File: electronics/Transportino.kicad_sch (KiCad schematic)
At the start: 44 parts

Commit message: Changed components and added new ones
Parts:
- removed C? (x10): 0.1u, symbol Device:C
- removed C? (x2): 1u, symbol Device:C
- removed J?: USB_B, symbol Connector:USB_B
- removed R? (x2): 27.4, symbol Device:R
- removed U?: RP2040, QFN40P700X700X90-57N, symbol RP2040:RP2040
- added BZ1: BUZZ, Buzzer_Beeper:Buzzer_12x9.5RM7.6, symbol Device:Buzzer
- added C1, C10, C11, C12, C14, C16, C23, C24, C5, C7, C8, C9: 0.1u, Capacitor_SMD:C_1206_3216Metric, symbol Device:C
- added C13, C15: 1u, Capacitor_SMD:C_1206_3216Metric, symbol Device:C
- added C20: 10n, Capacitor_SMD:C_1206_3216Metric, symbol Device:C
- added C26: 2.2n, Capacitor_SMD:C_1206_3216Metric, symbol Device:C
- added D2: STATUS, LED_SMD:LED_1206_3216Metric, symbol Device:LED
- added J1: MOTOR_A_0, Connector_JST:JST_XH_B3B-XH-A_1x03_P2.50mm_Vertical, symbol Connector:Conn_01x03_Female
- added J2: MOTOR_A_1, Connector_JST:JST_XH_B3B-XH-A_1x03_P2.50mm_Vertical, symbol Connector:Conn_01x03_Female
- added J3: MOTOR_B_0, Connector_JST:JST_XH_B3B-XH-A_1x03_P2.50mm_Vertical, symbol Connector:Conn_01x03_Female
- added J4: MOTOR_B_1, Connector_JST:JST_XH_B3B-XH-A_1x03_P2.50mm_Vertical, symbol Connector:Conn_01x03_Female
- added J5: USB_B_Micro, Connector_USB:USB_Micro-B_Amphenol_10118194_Horizontal, symbol Connector:USB_B_Micro
- added R1, R2: 27.4, Resistor_SMD:R_1206_3216Metric, symbol Device:R
- added R6: 1k, Resistor_SMD:R_1206_3216Metric, symbol Device:R
- added U1: RP2040, Package_DFN_QFN:QFN-56_EP_7.75x7.75_Pitch0.4mm, symbol RP2040:RP2040
- added U4: MPU-6050, Sensor_Motion:InvenSense_QFN-24_4x4mm_P0.5mm, symbol Sensor_Motion:MPU-6050
- BT1: renamed from BT?; footprint (none) -> Connector_JST:JST_XH_B2B-XH-A_1x02_P2.50mm_Vertical
- C17, C18, C19, C2, C22, C25, C4: renamed from C?; footprint (none) -> Capacitor_SMD:C_1206_3216Metric
- C21: renamed from C?; footprint (none) -> Capacitor_SMD:C_Elec_6.3x5.4
- C27: renamed from C?; footprint (none) -> Capacitor_SMD:C_Elec_8x10.2
- C3, C6: renamed from C?; footprint (none) -> Capacitor_SMD:CP_Elec_4x5.4
- D1: renamed from D?; value LED -> POWER; footprint (none) -> LED_SMD:LED_1206_3216Metric
- D3: renamed from D?; footprint DIOM6859X262N -> Diode_SMD:D_SMA
- L1: renamed from L?; footprint (none) -> Inductor_SMD:L_6.3x6.3_H3
- R3, R4, R7, R8, R9: renamed from R?; footprint (none) -> Resistor_SMD:R_1206_3216Metric
- R5: renamed from R?; value 4.7k -> 1k; footprint (none) -> Resistor_SMD:R_1206_3216Metric
- SW1: renamed from SW?; value SW_Push -> PROG; footprint (none) -> Button_Switch_SMD:SW_Push_SPST_NO_Alps_SKRK
- SW2: renamed from SW?; footprint (none) -> Button_Switch_THT:SW_CuK_OS102011MA1QN1_SPDT_Angled
- Y1: renamed from Y?; footprint (none) -> Crystal:Crystal_SMD_5032-4Pin_5.0x3.2mm
- gave numbers to parts that had none: 4
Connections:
- net +BATT is gone; now on net +12V: C21.1, U5.1 (VIN)
- net +1V1: now also C11.2, C13.2, C5.2, U1.23 (DVDD), U1.45 (VREG_VOUT), U1.50 (DVDD)
- net +3V3: now also D1.2 (A), C1.2, C10.2, C12.2, C14.2, C15.2, C16.2, C20.2, C23.2, C7.2, C8.2, C9.2, J2.2 (Pin_2), J4.2 (Pin_2), U1.1 (IOVDD), U1.10 (IOVDD), U1.22 (IOVDD), U1.33 (IOVDD), U1.42 (IOVDD), U1.43 (ADC_AVDD), U1.44 (VREG_VIN), U1.48 (USB_VDD), U1.49 (IOVDD), U4.13 (VDD), U4.8 (VDDIO)
- net +5V: no longer D1.1 (K)
- net CtrlA0: now also U1.28 (GPIO17)
- net CtrlA1: now also U1.29 (GPIO18)
- net CtrlAPWM: now also U1.27 (GPIO16)
- net CtrlB0: now also U1.34 (GPIO22)
- net CtrlB1: now also U1.35 (GPIO23)
- net CtrlBPWM: now also U1.32 (GPIO21)
- net DRV_EN: now also U1.18 (GPIO15)
- net GND: now also BZ1.2 (+), C1.1, C10.1, C11.1, C12.1, C13.1, C14.1, C15.1, C16.1, C20.1, C23.1, C24.1, C26.2, C5.1, C7.1, C8.1, C9.1, J2.3 (Pin_3), J4.3 (Pin_3), J5.5 (GND), J5.6 (Shield), R6.2, U1.19 (TESTEN), U1.57 (GND), U4.1 (CLKIN), U4.11 (FSYNC), U4.18 (GND)
- net MotorA0: now also J1.1 (Pin_1)
- net MotorA1: now also J1.2 (Pin_2)
- net MotorB0: now also J3.1 (Pin_1)
- net MotorB1: now also J3.2 (Pin_2)
- net QSPI_CSN: now also U1.56 (QSPI_SS_N)
- net QSPI_SCLK: now also U1.52 (QSPI_SCLK)
- net QSPI_SD0: now also U1.53 (QSPI_SD0)
- net QSPI_SD1: now also U1.55 (QSPI_SD1)
- net QSPI_SD2: now also U1.54 (QSPI_SD2)
- net QSPI_SD3: now also U1.51 (QSPI_SD3)
- net RUN: now also U1.26 (RUN)
- net SWCLK: now also U1.24 (SWCLK)
- net SWD: now also U1.25 (SWDIO)
- net USB_D+: now also J5.3 (D+), R1.2
- net USB_D-: now also J5.2 (D-), R2.2
- net VBUS: now also J5.1 (VBUS)
- net XIN: now also U1.20 (XIN)
- net XOUT: now also R3.2, U1.21 (XOUT); no longer R3.1
- net PROG_BTN: now reaches R4.1, SW1.2
- net at C18.1, Y1.2: now also R3.1; no longer R3.2
- net at R5.1: now also D1.1 (K); no longer D1.2 (A)
- net OUT: now reaches D3.C, L1.1, U5.2 (OUT)
- net VCC renamed BUCK_CONVERTER
- new net: C24.2, U4.10 (REGOUT)
- new net: D2.1 (K), R6.1
- new net: R2.1, U1.46 (USB_DM)
- new net: R1.1, U1.47 (USB_DP)
- new net: C26.1, U4.20 (CPOUT)
- new net AD0: U1.5 (GPIO3), U4.9 (AD0)
- new net BUZZ: BZ1.1 (-), U1.8 (GPIO6)
- new net INT: U1.4 (GPIO2), U4.12 (INT)
- new net MotorAENC0: J1.3 (Pin_3), U1.30 (GPIO19)
- new net MotorAENC1: J2.1 (Pin_1), U1.31 (GPIO20)
- new net MotorBENC0: J3.3 (Pin_3), U1.36 (GPIO24)
- new net MotorBENC1: J4.1 (Pin_1), U1.37 (GPIO25)
- new net SCL: U1.3 (GPIO1), U4.23 (SCL)
- new net SDA: U1.2 (GPIO0), U4.24 (SDA)
- new net STATUS_LED: D2.2 (A), U1.9 (GPIO7)
- new net XCL: U1.7 (GPIO5), U4.7 (AUX_SCL)
- new net XDA: U1.6 (GPIO4), U4.6 (AUX_SDA)
- no-connect marks 0 -> 12
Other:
- moved on the sheet: BT1, D1, R3, SW1

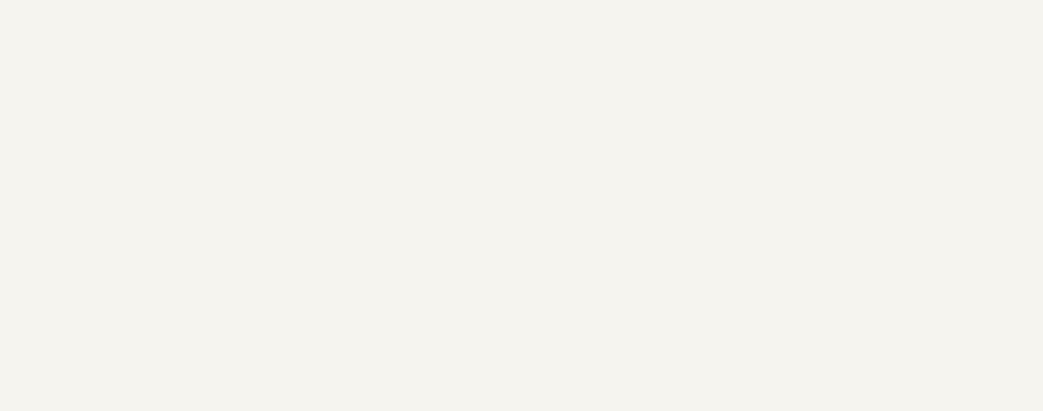
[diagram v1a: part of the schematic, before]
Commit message: Improved readme.md and added holes to mainboard
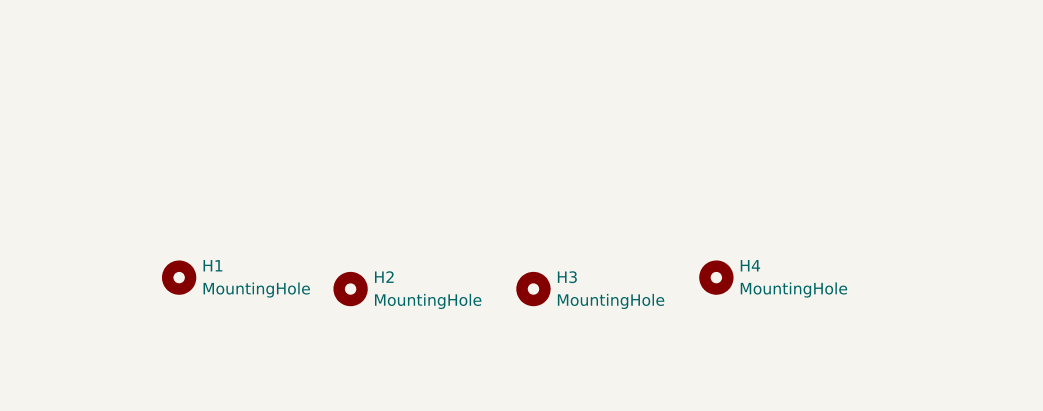
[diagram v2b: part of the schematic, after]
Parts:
- added H1, H2, H3, H4: MountingHole, MountingHole:MountingHole_2.2mm_M2, symbol Mechanical:MountingHole
- SW1: footprint Button_Switch_SMD:SW_Push_SPST_NO_Alps_SKRK -> Button_Switch_SMD:Button_SWITCH_6.1x3.7
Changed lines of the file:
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@@
     (property "Reference" "SW1" (id 0) (at 220.98 80.01 0))
     (property "Value" "PROG" (id 1) (at 220.98 82.55 0))
-    (property "Footprint" "Button_Switch_SMD:SW_Push_SPST_NO_Alps_SKRK" (id 2) (at 220.98 82.55 0)
+    (property "Footprint" "Button_Switch_SMD:Button_SWITCH_6.1x3.7" (id 2) (at 220.98 82.55 0)
       (effects (font (size 1.27 1.27)) hide)
     )
@@
     (pin "2")
   )
+  (symbol (lib_id "Mechanical:MountingHole") (at 111.76 259.08 0) (unit 1)
+    (in_bom yes) (on_board yes) (fields_autoplaced)
+    (property "Reference" "H2" (id 0) (at 114.3 257.8099 0)
+      (effects (font (size 1.27 1.27)) (justify left))
+    )
+    (property "Value" "MountingHole" (id 1) (at 114.3 260.3499 0)
+      (effects (font (size 1.27 1.27)) (justify left))
+    )
+    (property "Footprint" "MountingHole:MountingHole_2.2mm_M2" (id 2) (at 111.76 259.08 0)
+      (effects (font (size 1.27 1.27)) hide)
+    )
+    (property "Datasheet" "~" (id 3) (at 111.76 259.08 0)
+      (effects (font (size 1.27 1.27)) hide)
+    )
+  )
   (symbol (lib_id "power:GND") (at 50.8 171.45 0) (unit 1)
     (in_bom yes) (on_board yes)
@@
     )
     (pin "1")
+  )
+  (symbol (lib_id "Mechanical:MountingHole") (at 132.08 259.08 0) (unit 1)
+    (in_bom yes) (on_board yes) (fields_autoplaced)
+    (property "Reference" "H3" (id 0) (at 134.62 257.8099 0)
+      (effects (font (size 1.27 1.27)) (justify left))
+    )
+    (property "Value" "MountingHole" (id 1) (at 134.62 260.3499 0)
+      (effects (font (size 1.27 1.27)) (justify left))
+    )
+    (property "Footprint" "MountingHole:MountingHole_2.2mm_M2" (id 2) (at 132.08 259.08 0)
+      (effects (font (size 1.27 1.27)) hide)
+    )
+    (property "Datasheet" "~" (id 3) (at 132.08 259.08 0)
+      (effects (font (size 1.27 1.27)) hide)
+    )
   )
   (symbol (lib_id "power:+3V3") (at 189.23 48.26 270) (mirror x) (unit 1)
@@
     (pin "1")
   )
+  (symbol (lib_id "Mechanical:MountingHole") (at 152.4 257.81 0) (unit 1)
+    (in_bom yes) (on_board yes) (fields_autoplaced)
+    (property "Reference" "H4" (id 0) (at 154.94 256.5399 0)
+      (effects (font (size 1.27 1.27)) (justify left))
+    )
+    (property "Value" "MountingHole" (id 1) (at 154.94 259.0799 0)
+      (effects (font (size 1.27 1.27)) (justify left))
+    )
+    (property "Footprint" "MountingHole:MountingHole_2.2mm_M2" (id 2) (at 152.4 257.81 0)
+      (effects (font (size 1.27 1.27)) hide)
+    )
+    (property "Datasheet" "~" (id 3) (at 152.4 257.81 0)
+      (effects (font (size 1.27 1.27)) hide)
+    )
+  )
   (symbol (lib_id "power:+12V") (at 57.15 247.65 0) (unit 1)
     (in_bom yes) (on_board yes) (fields_autoplaced)
@@
     (pin "1")
   )
+  (symbol (lib_id "Mechanical:MountingHole") (at 92.71 257.81 0) (unit 1)
+    (in_bom yes) (on_board yes) (fields_autoplaced)
+    (property "Reference" "H1" (id 0) (at 95.25 256.5399 0)
+      (effects (font (size 1.27 1.27)) (justify left))
+    )
+    (property "Value" "MountingHole" (id 1) (at 95.25 259.0799 0)
+      (effects (font (size 1.27 1.27)) (justify left))
+    )
+    (property "Footprint" "MountingHole:MountingHole_2.2mm_M2" (id 2) (at 92.71 257.81 0)
+      (effects (font (size 1.27 1.27)) hide)
+    )
+    (property "Datasheet" "~" (id 3) (at 92.71 257.81 0)
+      (effects (font (size 1.27 1.27)) hide)
+    )
+  )
   (symbol (lib_id "Device:C_Polarized_US") (at 50.8 162.56 0) (unit 1)
     (in_bom yes) (on_board yes)
@@
       (reference "D3") (unit 1) (value "SS32") (footprint "Diode_SMD:D_SMA")
     )
+    (path "/f85a0141-6ff4-45de-aae6-298fd70a046a"
+      (reference "H1") (unit 1) (value "MountingHole") (footprint "MountingHole:MountingHole_2.2mm_M2")
+    )
+    (path "/66841c31-c845-4c94-96cd-2a7b74adbe0c"
+      (reference "H2") (unit 1) (value "MountingHole") (footprint "MountingHole:MountingHole_2.2mm_M2")
+    )
+    (path "/7b305265-4180-420c-8e15-e9ce60952f03"
+      (reference "H3") (unit 1) (value "MountingHole") (footprint "MountingHole:MountingHole_2.2mm_M2")
+    )
+    (path "/d1097040-5da8-496e-9ca2-6633d62b2369"
+      (reference "H4") (unit 1) (value "MountingHole") (footprint "MountingHole:MountingHole_2.2mm_M2")
+    )
     (path "/a19b516a-dc44-4576-a1ab-73e76e6f3f6f"
       (reference "J1") (unit 1) (value "MOTOR_A_0") (footprint "Connector_JST:JST_XH_B3B-XH-A_1x03_P2.50mm_Vertical")
@@
     )
     (path "/339c6356-b9db-49be-826a-6706286503f0"
-      (reference "SW1") (unit 1) (value "PROG") (footprint "Button_Switch_SMD:SW_Push_SPST_NO_Alps_SKRK")
+      (reference "SW1") (unit 1) (value "PROG") (footprint "Button_Switch_SMD:Button_SWITCH_6.1x3.7")
     )
     (path "/ba546255-5611-42ee-82d1-58b5bf876f4e"

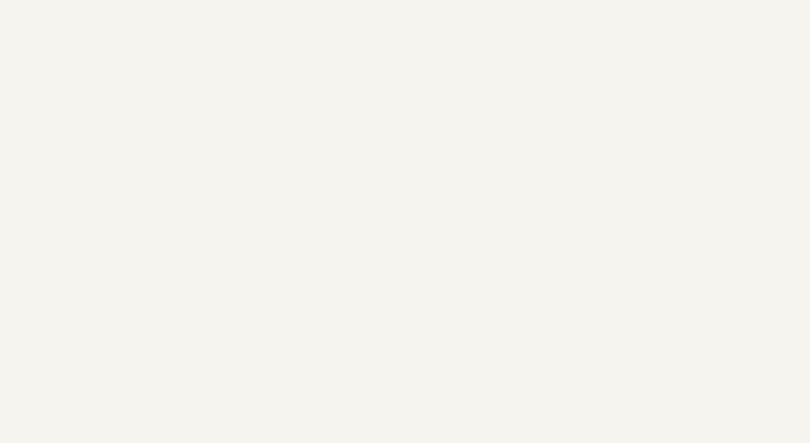
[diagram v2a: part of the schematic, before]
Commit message: Added link to the ArduCar repo
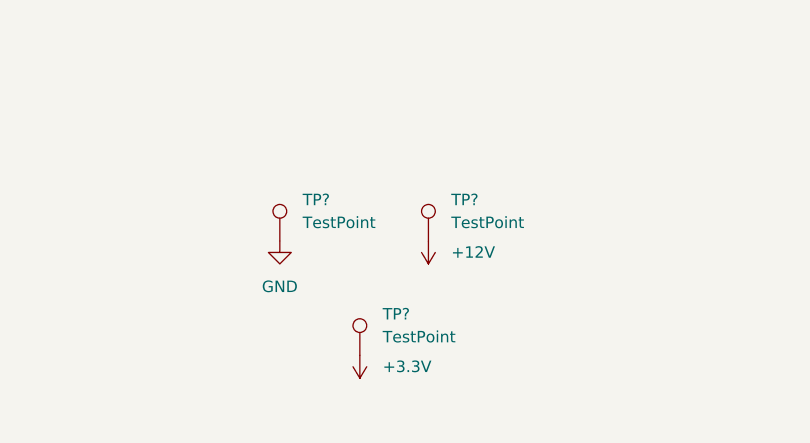
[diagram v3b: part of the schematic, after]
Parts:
- added TP? (x3): TestPoint, symbol Connector:TestPoint
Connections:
- net +12V: now also TP?.1
- net +3V3: now also TP?.1
- net GND: now also TP?.1
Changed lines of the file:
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@@
     (pin "2")
+  )
+  (symbol (lib_id "power:+12V") (at 247.65 250.19 180) (unit 1)
+    (in_bom yes) (on_board yes) (fields_autoplaced)
+    (property "Reference" "#PWR?" (id 0) (at 247.65 246.38 0)
+      (effects (font (size 1.27 1.27)) hide)
+    )
+    (property "Value" "+12V" (id 1) (at 250.19 251.4599 0)
+      (effects (font (size 1.27 1.27)) (justify right))
+    )
+    (property "Footprint" "" (id 2) (at 247.65 250.19 0)
+      (effects (font (size 1.27 1.27)) hide)
+    )
+    (property "Datasheet" "" (id 3) (at 247.65 250.19 0)
+      (effects (font (size 1.27 1.27)) hide)
+    )
+    (pin "1")
   )
   (symbol (lib_id "power:GND") (at 330.2 88.9 0) (unit 1)
@@
     (pin "2")
   )
+  (symbol (lib_id "Connector:TestPoint") (at 231.14 250.19 0) (unit 1)
+    (in_bom yes) (on_board yes) (fields_autoplaced)
+    (property "Reference" "TP?" (id 0) (at 233.68 245.6179 0)
+      (effects (font (size 1.27 1.27)) (justify left))
+    )
+    (property "Value" "TestPoint" (id 1) (at 233.68 248.1579 0)
+      (effects (font (size 1.27 1.27)) (justify left))
+    )
+    (property "Footprint" "" (id 2) (at 236.22 250.19 0)
+      (effects (font (size 1.27 1.27)) hide)
+    )
+    (property "Datasheet" "~" (id 3) (at 236.22 250.19 0)
+      (effects (font (size 1.27 1.27)) hide)
+    )
+    (pin "1")
+  )
   (symbol (lib_id "power:GND") (at 347.98 93.98 0) (unit 1)
     (in_bom yes) (on_board yes) (fields_autoplaced)
@@
     (pin "2")
   )
+  (symbol (lib_id "Connector:TestPoint") (at 247.65 250.19 0) (unit 1)
+    (in_bom yes) (on_board yes) (fields_autoplaced)
+    (property "Reference" "TP?" (id 0) (at 250.19 245.6179 0)
+      (effects (font (size 1.27 1.27)) (justify left))
+    )
+    (property "Value" "TestPoint" (id 1) (at 250.19 248.1579 0)
+      (effects (font (size 1.27 1.27)) (justify left))
+    )
+    (property "Footprint" "" (id 2) (at 252.73 250.19 0)
+      (effects (font (size 1.27 1.27)) hide)
+    )
+    (property "Datasheet" "~" (id 3) (at 252.73 250.19 0)
+      (effects (font (size 1.27 1.27)) hide)
+    )
+    (pin "1")
+  )
   (symbol (lib_id "power:+3V3") (at 342.9 123.19 0) (unit 1)
     (in_bom yes) (on_board yes) (fields_autoplaced)
@@
     (pin "5")
   )
+  (symbol (lib_id "Connector:TestPoint") (at 240.03 262.89 0) (unit 1)
+    (in_bom yes) (on_board yes) (fields_autoplaced)
+    (property "Reference" "TP?" (id 0) (at 242.57 258.3179 0)
+      (effects (font (size 1.27 1.27)) (justify left))
+    )
+    (property "Value" "TestPoint" (id 1) (at 242.57 260.8579 0)
+      (effects (font (size 1.27 1.27)) (justify left))
+    )
+    (property "Footprint" "" (id 2) (at 245.11 262.89 0)
+      (effects (font (size 1.27 1.27)) hide)
+    )
+    (property "Datasheet" "~" (id 3) (at 245.11 262.89 0)
+      (effects (font (size 1.27 1.27)) hide)
+    )
+    (pin "1")
+  )
   (symbol (lib_id "power:GND") (at 323.85 127 270) (unit 1)
     (in_bom yes) (on_board yes) (fields_autoplaced)
@@
     (pin "2")
   )
+  (symbol (lib_id "power:+3.3V") (at 240.03 262.89 180) (unit 1)
+    (in_bom yes) (on_board yes) (fields_autoplaced)
+    (property "Reference" "#PWR?" (id 0) (at 240.03 259.08 0)
+      (effects (font (size 1.27 1.27)) hide)
+    )
+    (property "Value" "+3.3V" (id 1) (at 242.57 264.1599 0)
+      (effects (font (size 1.27 1.27)) (justify right))
+    )
+    (property "Footprint" "" (id 2) (at 240.03 262.89 0)
+      (effects (font (size 1.27 1.27)) hide)
+    )
+    (property "Datasheet" "" (id 3) (at 240.03 262.89 0)
+      (effects (font (size 1.27 1.27)) hide)
+    )
+    (pin "1")
+  )
+  (symbol (lib_id "power:GND") (at 231.14 250.19 0) (unit 1)
+    (in_bom yes) (on_board yes) (fields_autoplaced)
+    (property "Reference" "#PWR08" (id 0) (at 231.14 256.54 0)
+      (effects (font (size 1.27 1.27)) hide)
+    )
+    (property "Value" "GND" (id 1) (at 231.14 255.27 0))
+    (property "Footprint" "" (id 2) (at 231.14 250.19 0)
+      (effects (font (size 1.27 1.27)) hide)
+    )
+    (property "Datasheet" "" (id 3) (at 231.14 250.19 0)
+      (effects (font (size 1.27 1.27)) hide)
+    )
+    (pin "1")
+  )
   (symbol (lib_id "power:GND") (at 152.4 78.74 0) (mirror y) (unit 1)
     (in_bom yes) (on_board yes)
@@
       (reference "#PWR07") (unit 1) (value "GND") (footprint "")
     )
+    (path "/f53751bf-3f01-46a2-b759-057b4c0f038b"
+      (reference "#PWR08") (unit 1) (value "GND") (footprint "")
+    )
     (path "/7173b8de-f2cd-4b2e-a737-630c5879ec74"
       (reference "#PWR011") (unit 1) (value "GND") (footprint "")
@@
       (reference "#PWR0125") (unit 1) (value "+3V3") (footprint "")
     )
+    (path "/20ac7f1d-5328-42f9-b97e-8392aa4624bf"
+      (reference "#PWR?") (unit 1) (value "+12V") (footprint "")
+    )
+    (path "/f52161a0-f4fe-4469-bc3c-f014e7fd5873"
+      (reference "#PWR?") (unit 1) (value "+3.3V") (footprint "")
+    )
     (path "/897e7ab0-9b87-49aa-9009-a8e87aac9abb"
       (reference "BT1") (unit 1) (value "Battery") (footprint "Connector_JST:JST_XH_B2B-XH-A_1x02_P2.50mm_Vertical")
@@
       (reference "SW2") (unit 1) (value "SW_DPDT_x2") (footprint "Button_Switch_THT:SW_CuK_OS102011MA1QN1_SPDT_Angled")
     )
+    (path "/9826bb83-0155-4d11-a9af-8e66989debcc"
+      (reference "TP?") (unit 1) (value "TestPoint") (footprint "")
+    )
+    (path "/c77cc684-6d7d-40ca-80fb-70970ffcddef"
+      (reference "TP?") (unit 1) (value "TestPoint") (footprint "")
+    )
+    (path "/f01d4561-db8e-400b-b14c-0fc04801d7f5"
+      (reference "TP?") (unit 1) (value "TestPoint") (footprint "")
+    )
     (path "/57fde7d1-ea1d-4cdd-9e7c-ae005a61eb86"
